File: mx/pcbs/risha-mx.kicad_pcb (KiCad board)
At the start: 2 copper layers, 100 x 95.3 mm, 19 parts

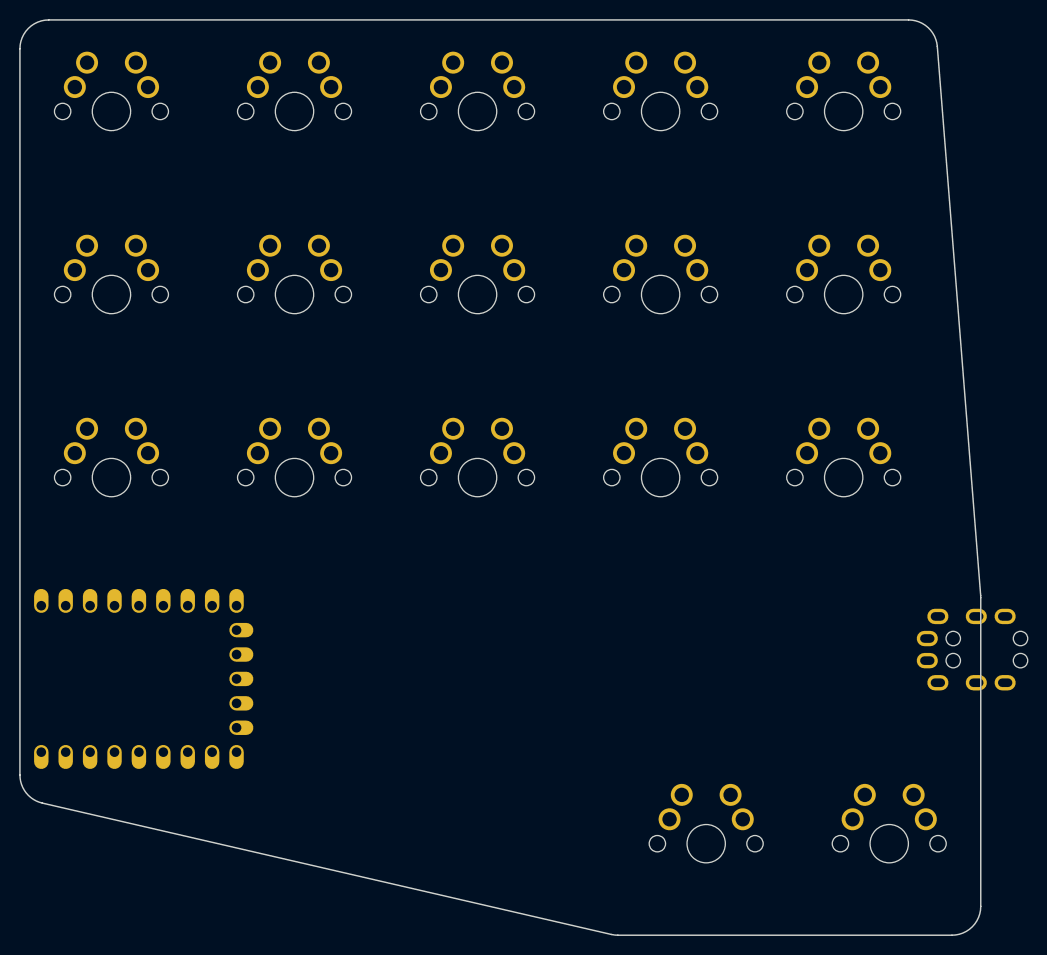
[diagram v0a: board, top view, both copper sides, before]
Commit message: tweak outline for MX version
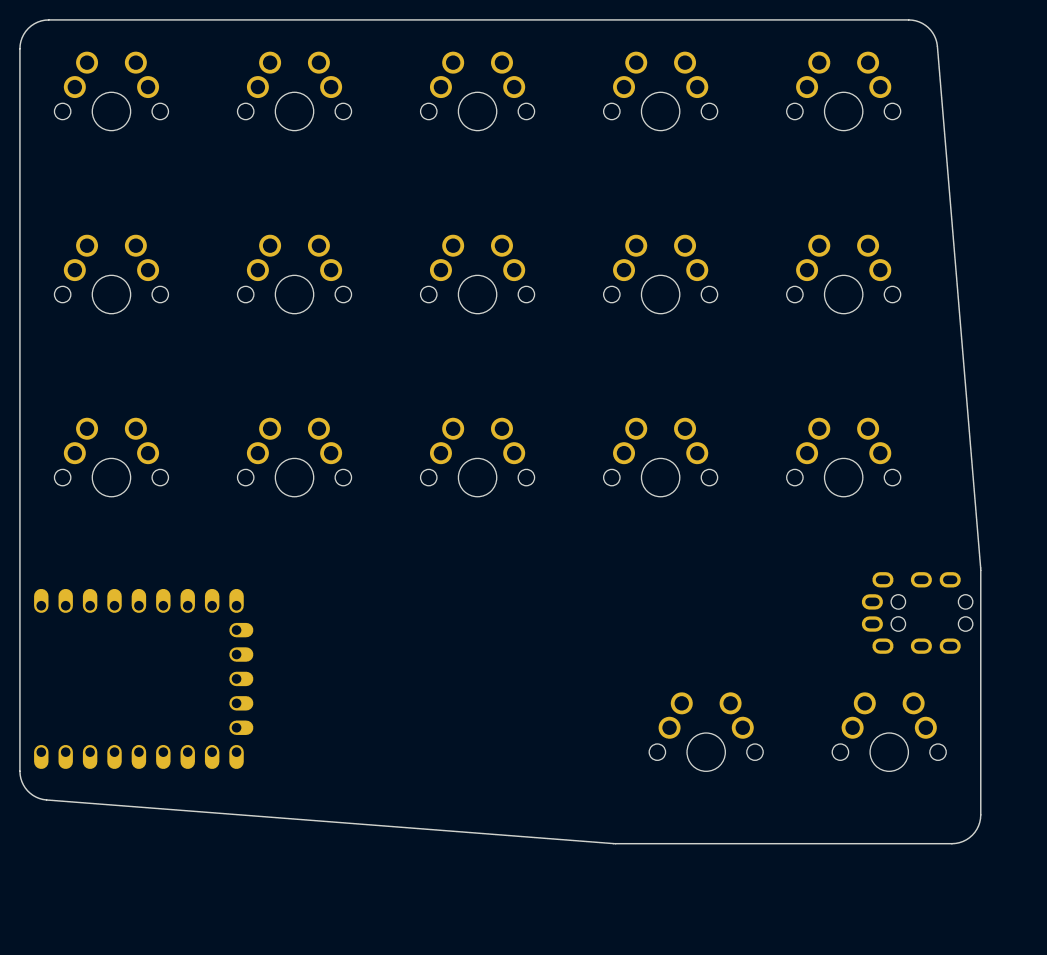
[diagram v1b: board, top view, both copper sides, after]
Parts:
- moved S16 9.53 mm to (214.3, 181.0)
- moved S17 9.53 mm to (233.3, 181.0)
- moved TRRS1 6.87 mm to (242.9, 167.6)
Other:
- board size 100 x 95.3 mm -> 100 x 85.7 mm
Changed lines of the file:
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@@
           )
       (module MX (layer F.Cu)
-      (at 214.29000000000002 190.5 0)
+      (at 214.29000000000002 180.975 0)
       (fp_text reference "S16" (at 0 0) (layer F.SilkS) hide (effects (font (size 1.27 1.27) (thickness 0.15))))
       (fp_text value "" (at 0 0) (layer F.SilkS) hide (effects (font (size 1.27 1.27) (thickness 0.15))))
@@
           )
       (module MX (layer F.Cu)
-      (at 233.34000000000003 190.5 0)
+      (at 233.34000000000003 180.975 0)
       (fp_text reference "S17" (at 0 0) (layer F.SilkS) hide (effects (font (size 1.27 1.27) (thickness 0.15))))
       (fp_text value "" (at 0 0) (layer F.SilkS) hide (effects (font (size 1.27 1.27) (thickness 0.15))))
@@
     )
       (module TRRS-PJ-320A-dual (layer F.Cu)
-      (at 248.60250000000002 171.45000000000002 270)
+      (at 242.88750000000002 167.64000000000001 270)
       (fp_text reference "TRRS1" (at 0 14.2) (layer Dwgs.User) (effects (font (size 1 1) (thickness 0.15))))
       (fp_text value TRRS-PJ-320A-dual (at 0 -5.6) (layer F.Fab) (effects (font (size 1 1) (thickness 0.15))))
@@
         (pad 4 thru_hole oval (at -4.6 3.2 270) (size 1.6 2.2) (drill oval 0.9 1.5) (layers *.Cu *.Mask) (net 19 "GP8"))
       )
-            (gr_line (start 142.875 183.35115725804656) (end 142.875 107.77499999999999) (angle 90) (layer Edge.Cuts) (width 0.15))
-(gr_line (start 145.875 104.77499999999999) (end 235.35262578572684 104.77499999999999) (angle 90) (layer Edge.Cuts) (width 0.15))
-(gr_line (start 238.34331019357685 107.53876559937999) (end 242.85568440785002 164.6645663721647) (angle 90) (layer Edge.Cuts) (width 0.15))
-(gr_line (start 242.865 164.9008007727848) (end 242.865 197.025) (angle 90) (layer Edge.Cuts) (width 0.15))
-(gr_line (start 239.865 200.025) (end 205.10678493784775 200.025) (angle 90) (layer Edge.Cuts) (width 0.15))
-(gr_line (start 204.43197365470533 199.94811982697692) (end 145.20018871685755 186.2742770850235) (angle 90) (layer Edge.Cuts) (width 0.15))
+            (gr_line (start 142.875 182.9594839973703) (end 142.875 107.77499999999999) (angle 90) (layer Edge.Cuts) (width 0.15))
+(gr_line (start 145.875 104.77499999999999) (end 235.36351806430451 104.77499999999999) (angle 90) (layer Edge.Cuts) (width 0.15))
+(gr_line (start 238.35325257322495 107.52703260755379) (end 242.85473450892053 161.80122936388307) (angle 90) (layer Edge.Cuts) (width 0.15))
+(gr_line (start 242.86500000000004 162.04919675632937) (end 242.86500000000004 187.5) (angle 90) (layer Edge.Cuts) (width 0.15))
+(gr_line (start 239.86500000000004 190.5) (end 204.8802567774803 190.5) (angle 90) (layer Edge.Cuts) (width 0.15))
+(gr_line (start 204.65008418454144 190.49115710823847) (end 145.64482740706114 185.9506411056088) (angle 90) (layer Edge.Cuts) (width 0.15))
 (gr_arc (start 145.875 107.77499999999999) (end 145.875 104.77499999999999) (angle -90) (layer Edge.Cuts) (width 0.15))
-(gr_arc (start 235.35262578572684 107.77499999999999) (end 238.34331018572684 107.53876559999999) (angle -85.48357951525956) (layer Edge.Cuts) (width 0.15))
-(gr_arc (start 239.865 164.9008007727848) (end 242.865 164.9008007727848) (angle -4.516420484742325) (layer Edge.Cuts) (width 0.15))
-(gr_arc (start 239.865 197.025) (end 239.865 200.025) (angle -90) (layer Edge.Cuts) (width 0.15))
-(gr_arc (start 205.10678493784775 197.025) (end 204.43197363784776 199.9481199) (angle -12.999179268914816) (layer Edge.Cuts) (width 0.15))
-(gr_arc (start 145.875 183.35115725804656) (end 142.875 183.35115725804656) (angle -77.00082073108479) (layer Edge.Cuts) (width 0.15))
+(gr_arc (start 235.36351806430451 107.77499999999999) (end 238.3532525643045 107.5270326) (angle -85.25876255983361) (layer Edge.Cuts) (width 0.15))
+(gr_arc (start 239.86500000000004 162.04919675632937) (end 242.86500000000004 162.04919675632937) (angle -4.7412374401682) (layer Edge.Cuts) (width 0.15))
+(gr_arc (start 239.86500000000004 187.5) (end 239.86500000000004 190.5) (angle -90) (layer Edge.Cuts) (width 0.15))
+(gr_arc (start 204.8802567774803 187.5) (end 204.6500841774803 190.4911571) (angle -4.400297001419915) (layer Edge.Cuts) (width 0.15))
+(gr_arc (start 145.875 182.9594839973703) (end 142.875 182.9594839973703) (angle -85.59970299858014) (layer Edge.Cuts) (width 0.15))
 )

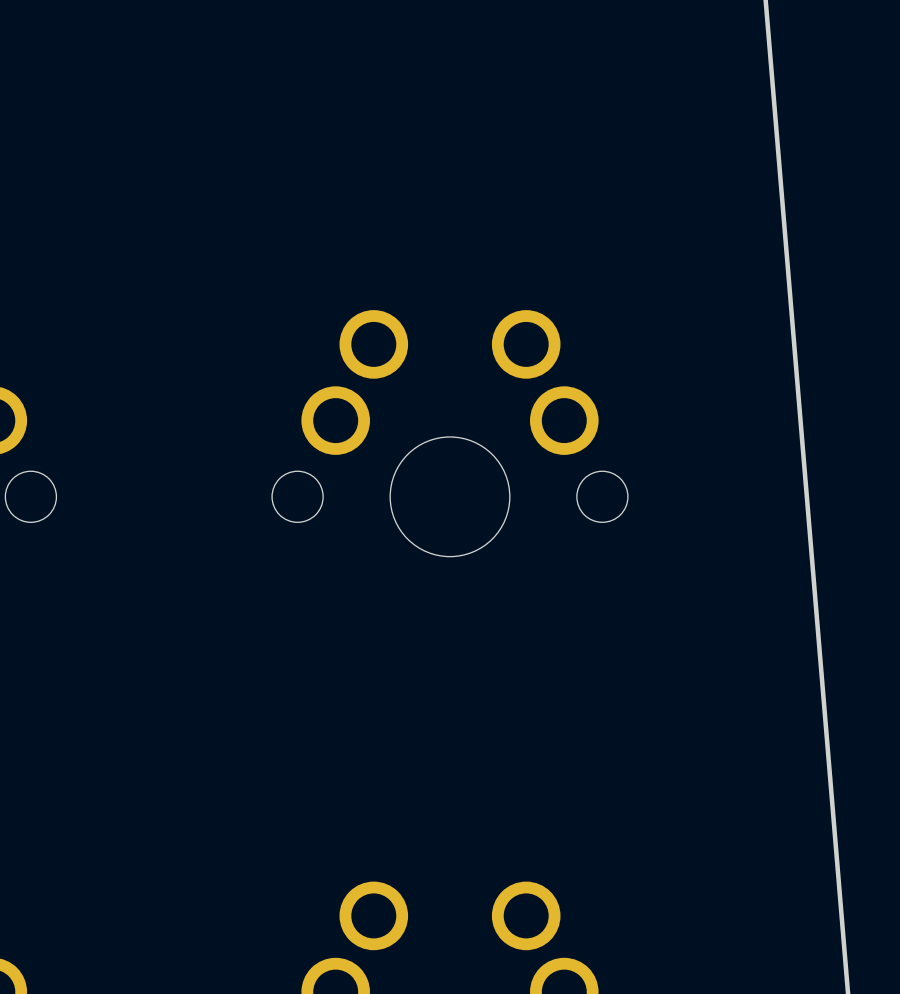
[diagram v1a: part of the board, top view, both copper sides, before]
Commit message: adding version and JLC text
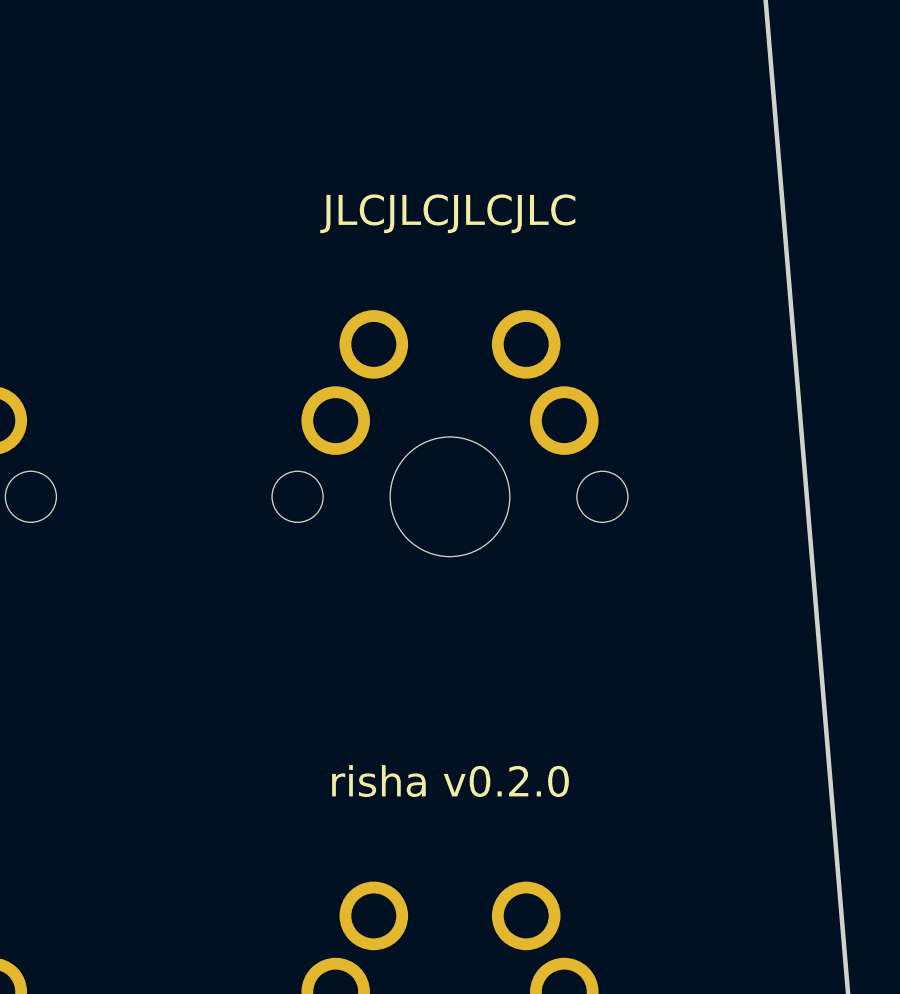
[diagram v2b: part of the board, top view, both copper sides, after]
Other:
- board text added: "JLCJLCJLCJLC"
- board text added: "risha v0.2.0"
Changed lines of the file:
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@@
         (pad 4 thru_hole oval (at -4.6 3.2 270) (size 1.6 2.2) (drill oval 0.9 1.5) (layers *.Cu *.Mask) (net 19 "GP8"))
       )
+            (gr_text "JLCJLCJLCJLC" (at 228.60000000000002 123.825 0) (layer F.SilkS)
+                (effects (font (size 1 1) (thickness 0.15)) )
+            )
+            (gr_text "risha v0.2.0" (at 228.60000000000002 142.875 0) (layer F.SilkS)
+                (effects (font (size 1 1) (thickness 0.15)) )
+            )
             (gr_line (start 142.875 182.9594839973703) (end 142.875 107.77499999999999) (angle 90) (layer Edge.Cuts) (width 0.15))
 (gr_line (start 145.875 104.77499999999999) (end 235.36351806430451 104.77499999999999) (angle 90) (layer Edge.Cuts) (width 0.15))

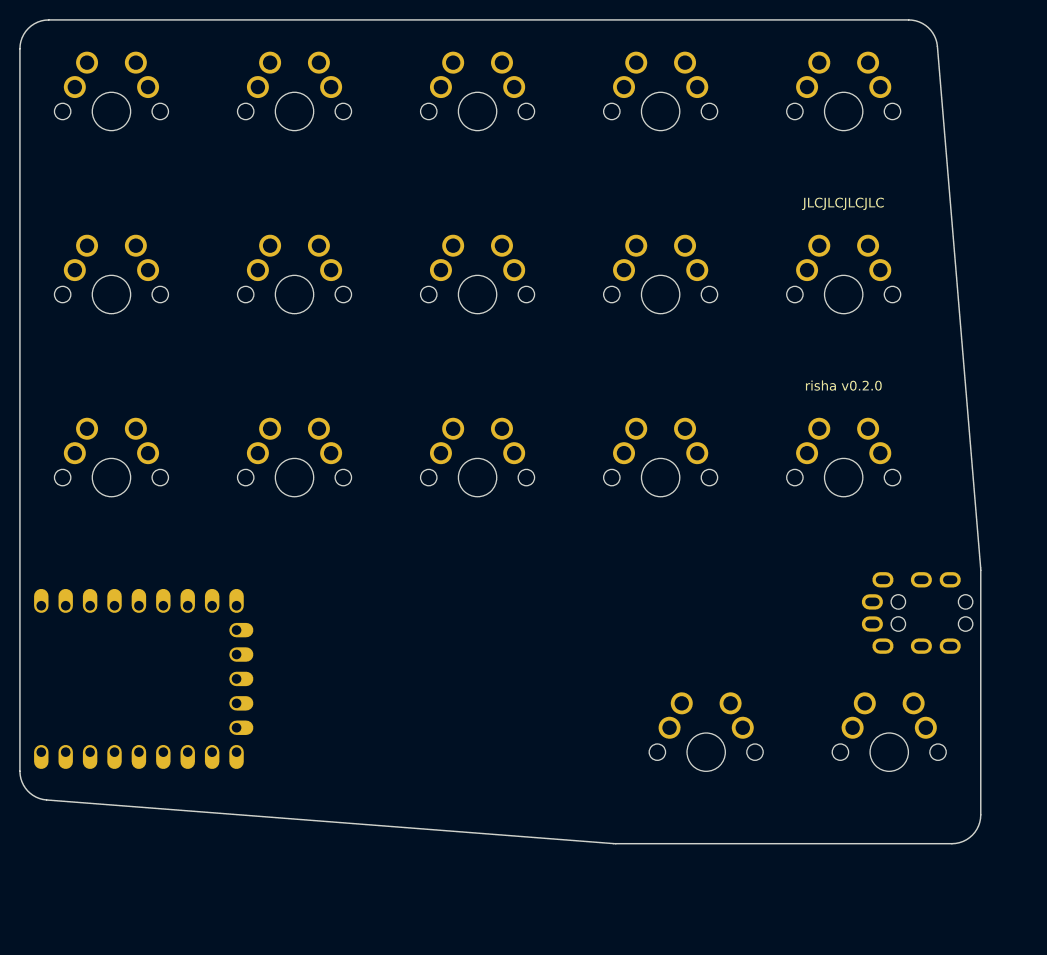
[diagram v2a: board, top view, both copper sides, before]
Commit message: drop mx thumb cluster a little lower
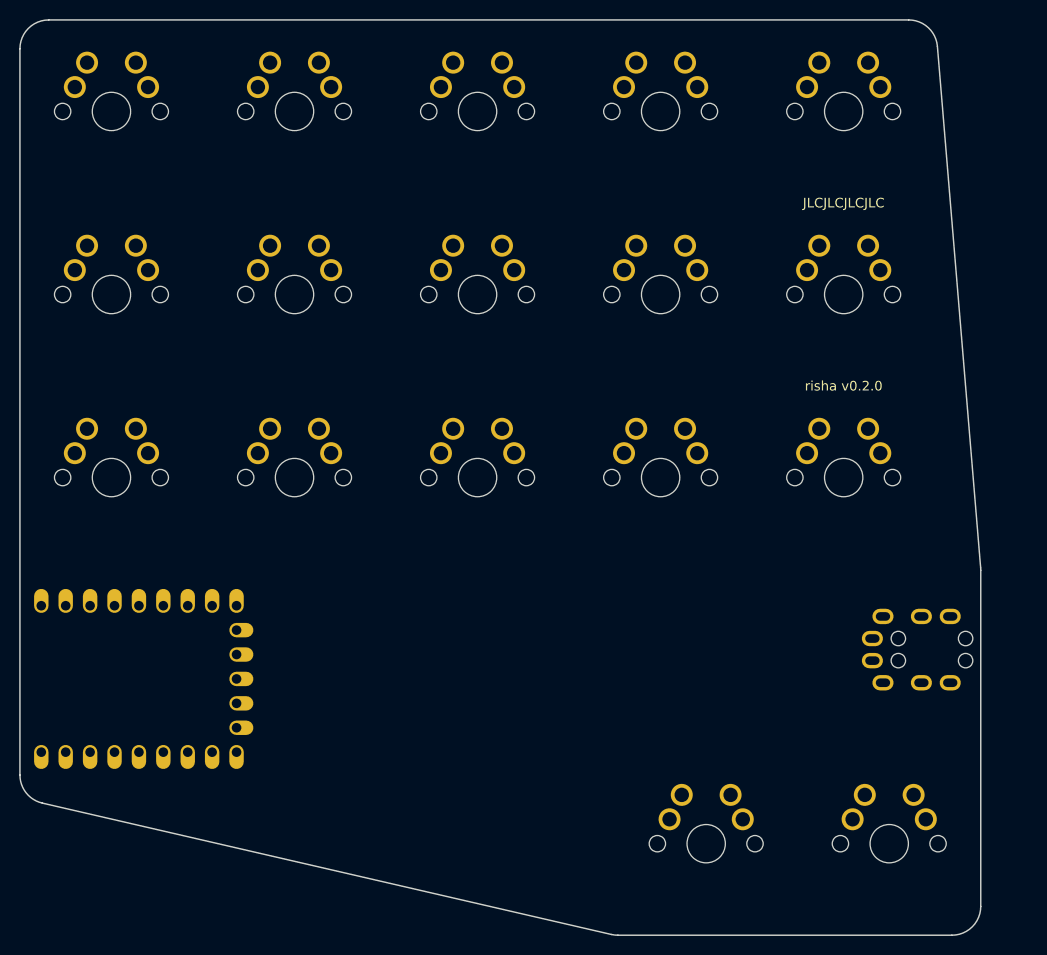
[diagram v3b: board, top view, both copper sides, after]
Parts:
- moved S16 9.53 mm to (214.3, 190.5)
- moved S17 9.53 mm to (233.3, 190.5)
- moved TRRS1 3.81 mm to (242.9, 171.5)
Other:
- board size 100 x 85.7 mm -> 100 x 95.3 mm
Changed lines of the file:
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@@
           )
       (module MX (layer F.Cu)
-      (at 214.29000000000002 180.975 0)
+      (at 214.29000000000002 190.5 0)
       (fp_text reference "S16" (at 0 0) (layer F.SilkS) hide (effects (font (size 1.27 1.27) (thickness 0.15))))
       (fp_text value "" (at 0 0) (layer F.SilkS) hide (effects (font (size 1.27 1.27) (thickness 0.15))))
@@
           )
       (module MX (layer F.Cu)
-      (at 233.34000000000003 180.975 0)
+      (at 233.34000000000003 190.5 0)
       (fp_text reference "S17" (at 0 0) (layer F.SilkS) hide (effects (font (size 1.27 1.27) (thickness 0.15))))
       (fp_text value "" (at 0 0) (layer F.SilkS) hide (effects (font (size 1.27 1.27) (thickness 0.15))))
@@
     )
       (module TRRS-PJ-320A-dual (layer F.Cu)
-      (at 242.88750000000002 167.64000000000001 270)
+      (at 242.88750000000002 171.45000000000002 270)
       (fp_text reference "TRRS1" (at 0 14.2) (layer Dwgs.User) (effects (font (size 1 1) (thickness 0.15))))
       (fp_text value TRRS-PJ-320A-dual (at 0 -5.6) (layer F.Fab) (effects (font (size 1 1) (thickness 0.15))))
@@
                 (effects (font (size 1 1) (thickness 0.15)) )
             )
-            (gr_line (start 142.875 182.9594839973703) (end 142.875 107.77499999999999) (angle 90) (layer Edge.Cuts) (width 0.15))
-(gr_line (start 145.875 104.77499999999999) (end 235.36351806430451 104.77499999999999) (angle 90) (layer Edge.Cuts) (width 0.15))
-(gr_line (start 238.35325257322495 107.52703260755379) (end 242.85473450892053 161.80122936388307) (angle 90) (layer Edge.Cuts) (width 0.15))
-(gr_line (start 242.86500000000004 162.04919675632937) (end 242.86500000000004 187.5) (angle 90) (layer Edge.Cuts) (width 0.15))
-(gr_line (start 239.86500000000004 190.5) (end 204.8802567774803 190.5) (angle 90) (layer Edge.Cuts) (width 0.15))
-(gr_line (start 204.65008418454144 190.49115710823847) (end 145.64482740706114 185.9506411056088) (angle 90) (layer Edge.Cuts) (width 0.15))
+            (gr_line (start 142.875 183.35115725804656) (end 142.875 107.77499999999999) (angle 90) (layer Edge.Cuts) (width 0.15))
+(gr_line (start 145.875 104.77499999999999) (end 235.3635180643045 104.77499999999999) (angle 90) (layer Edge.Cuts) (width 0.15))
+(gr_line (start 238.35325257322498 107.52703260755379) (end 242.85473450892053 161.80122936388307) (angle 90) (layer Edge.Cuts) (width 0.15))
+(gr_line (start 242.86500000000004 162.0491967563289) (end 242.86500000000004 197.025) (angle 90) (layer Edge.Cuts) (width 0.15))
+(gr_line (start 239.86500000000004 200.025) (end 205.10678493784775 200.025) (angle 90) (layer Edge.Cuts) (width 0.15))
+(gr_line (start 204.43197365470533 199.94811982697692) (end 145.20018871685755 186.2742770850235) (angle 90) (layer Edge.Cuts) (width 0.15))
 (gr_arc (start 145.875 107.77499999999999) (end 145.875 104.77499999999999) (angle -90) (layer Edge.Cuts) (width 0.15))
-(gr_arc (start 235.36351806430451 107.77499999999999) (end 238.3532525643045 107.5270326) (angle -85.25876255983361) (layer Edge.Cuts) (width 0.15))
-(gr_arc (start 239.86500000000004 162.04919675632937) (end 242.86500000000004 162.04919675632937) (angle -4.7412374401682) (layer Edge.Cuts) (width 0.15))
-(gr_arc (start 239.86500000000004 187.5) (end 239.86500000000004 190.5) (angle -90) (layer Edge.Cuts) (width 0.15))
-(gr_arc (start 204.8802567774803 187.5) (end 204.6500841774803 190.4911571) (angle -4.400297001419915) (layer Edge.Cuts) (width 0.15))
-(gr_arc (start 145.875 182.9594839973703) (end 142.875 182.9594839973703) (angle -85.59970299858014) (layer Edge.Cuts) (width 0.15))
+(gr_arc (start 235.3635180643045 107.77499999999999) (end 238.35325256430448 107.5270326) (angle -85.25876255983368) (layer Edge.Cuts) (width 0.15))
+(gr_arc (start 239.86500000000004 162.0491967563289) (end 242.86500000000004 162.0491967563289) (angle -4.741237440159549) (layer Edge.Cuts) (width 0.15))
+(gr_arc (start 239.86500000000004 197.025) (end 239.86500000000004 200.025) (angle -90) (layer Edge.Cuts) (width 0.15))
+(gr_arc (start 205.10678493784775 197.025) (end 204.43197363784776 199.9481199) (angle -12.999179268914816) (layer Edge.Cuts) (width 0.15))
+(gr_arc (start 145.875 183.35115725804656) (end 142.875 183.35115725804656) (angle -77.00082073108479) (layer Edge.Cuts) (width 0.15))
 )
